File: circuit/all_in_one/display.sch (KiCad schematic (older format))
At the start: 8 parts, among them U10 IN-14, U11 IN-14, U12 IN-14, U13 IN-14, U14 IN-14, U15 IN-14, U16 IN-14, U17 IN-14

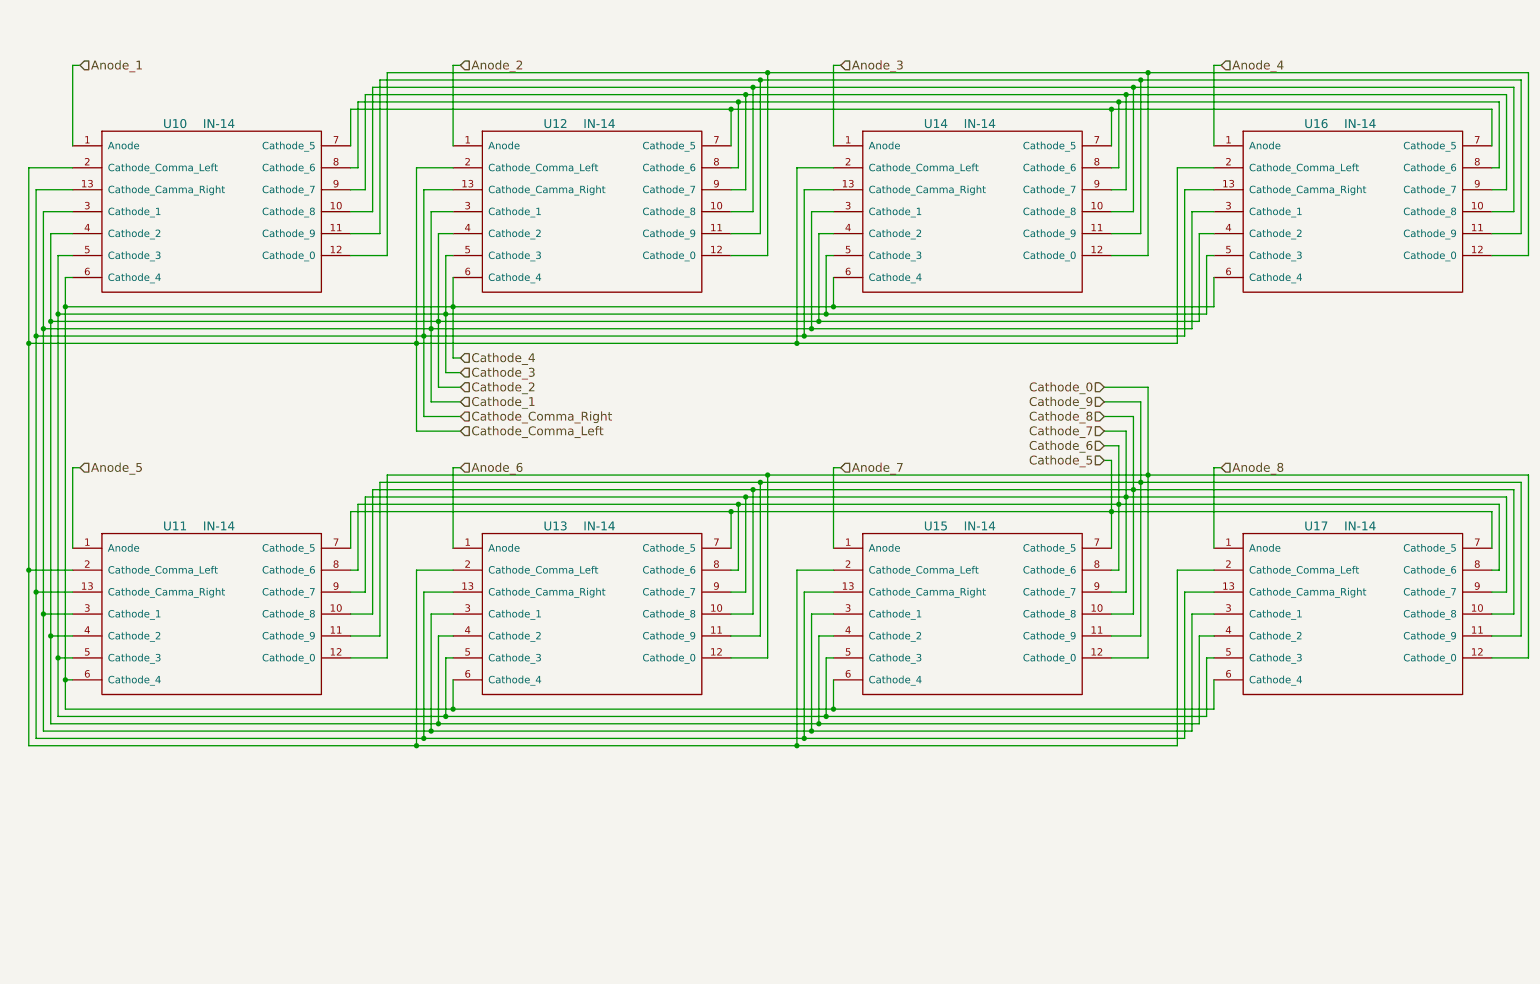
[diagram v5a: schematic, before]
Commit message: Finsihed placing all the components
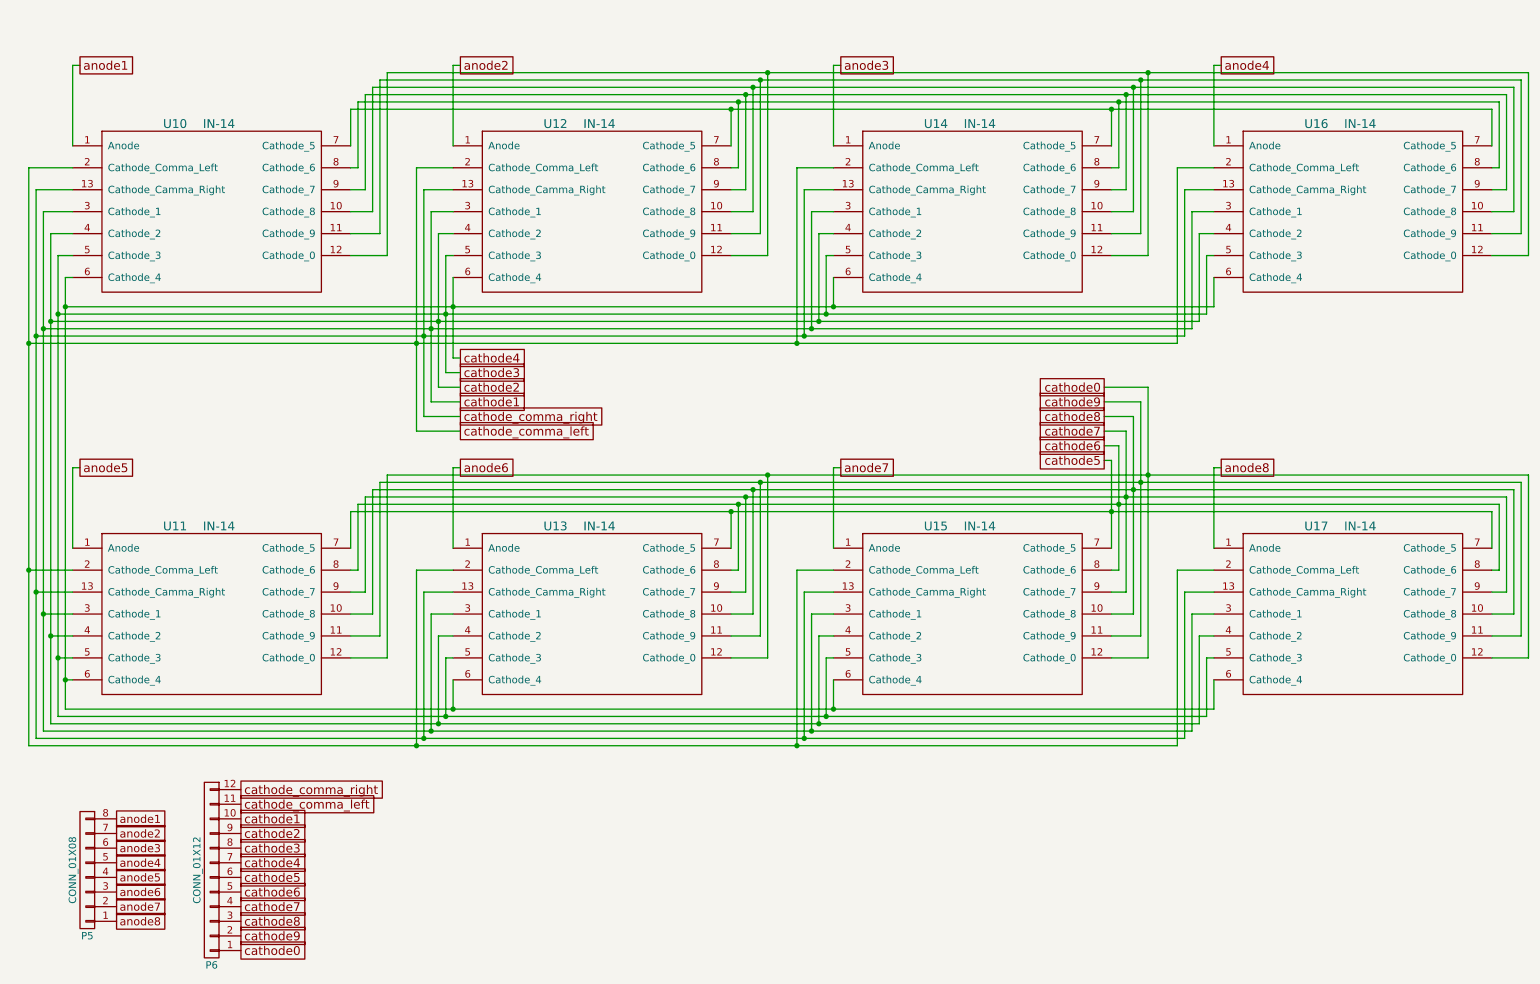
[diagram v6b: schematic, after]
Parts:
- added P5: CONN_01X08, Pin_Headers:Pin_Header_Straight_1x08, symbol CONN_01X08
- added P6: CONN_01X12, Pin_Headers:Pin_Header_Straight_1x12, symbol CONN_01X12
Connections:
- net Anode_1 renamed anode1
- net anode1: now also P5.8 (P8)
- net Anode_2 renamed anode2
- net anode2: now also P5.7 (P7)
- net Anode_3 renamed anode3
- net anode3: now also P5.6 (P6)
- net Anode_4 renamed anode4
- net anode4: now also P5.5 (P5)
- net Anode_5 renamed anode5
- net anode5: now also P5.4 (P4)
- net Anode_6 renamed anode6
- net anode6: now also P5.3 (P3)
- net Anode_7 renamed anode7
- net anode7: now also P5.2 (P2)
- net Anode_8 renamed anode8
- net anode8: now also P5.1 (P1)
- net Cathode_0 renamed cathode0
- net cathode0: now also P6.1 (P1)
- net Cathode_1 renamed cathode1
- net cathode1: now also P6.10 (P10)
- net Cathode_2 renamed cathode2
- net cathode2: now also P6.9 (P9)
- net Cathode_3 renamed cathode3
- net cathode3: now also P6.8 (P8)
- net Cathode_4 renamed cathode4
- net cathode4: now also P6.7 (P7)
- net Cathode_5 renamed cathode5
- net cathode5: now also P6.6 (P6)
- net Cathode_6 renamed cathode6
- net cathode6: now also P6.5 (P5)
- net Cathode_7 renamed cathode7
- net cathode7: now also P6.4 (P4)
- net Cathode_8 renamed cathode8
- net cathode8: now also P6.3 (P3)
- net Cathode_9 renamed cathode9
- net cathode9: now also P6.2 (P2)
- net Cathode_Comma_Left renamed cathode_comma_left
- net cathode_comma_left: now also P6.11 (P11)
- net Cathode_Comma_Right renamed cathode_comma_right
- net cathode_comma_right: now also P6.12 (P12)
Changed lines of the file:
@@
 $Descr A4 11693 8268
 encoding utf-8
-Sheet 6 6
+Sheet 6 5
 Title ""
 Date ""
@@
 Wire Wire Line
 	3150 5250 3150 4000
-Wire Wire Line
-	3150 4000 10950 4000
 Wire Wire Line
 	5750 4000 5750 5250
@@
 Wire Wire Line
 	3600 1750 3600 1200
-Text HLabel 3650 1200 2    60   Input ~ 0
-Anode_2
 Wire Wire Line
 	3600 1200 3650 1200
 Wire Wire Line
 	1000 1750 1000 1200
-Text HLabel 1050 1200 2    60   Input ~ 0
-Anode_1
 Wire Wire Line
 	1000 1200 1050 1200
 Wire Wire Line
 	6200 1750 6200 1200
-Text HLabel 6250 1200 2    60   Input ~ 0
-Anode_3
 Wire Wire Line
 	6200 1200 6250 1200
 Wire Wire Line
 	8800 1750 8800 1200
-Text HLabel 8850 1200 2    60   Input ~ 0
-Anode_4
 Wire Wire Line
 	8800 1200 8850 1200
 Wire Wire Line
 	1000 4500 1000 3950
-Text HLabel 1050 3950 2    60   Input ~ 0
-Anode_5
 Wire Wire Line
 	1000 3950 1050 3950
 Wire Wire Line
 	3600 4500 3600 3950
-Text HLabel 3650 3950 2    60   Input ~ 0
-Anode_6
 Wire Wire Line
 	3600 3950 3650 3950
 Wire Wire Line
 	6200 4500 6200 3950
-Text HLabel 6250 3950 2    60   Input ~ 0
-Anode_7
 Wire Wire Line
 	6200 3950 6250 3950
 Wire Wire Line
 	8800 4500 8800 3950
-Text HLabel 8850 3950 2    60   Input ~ 0
-Anode_8
 Wire Wire Line
 	8800 3950 8850 3950
-Text HLabel 3650 3200 2    60   Input ~ 0
-Cathode_4
-Text HLabel 3650 3300 2    60   Input ~ 0
-Cathode_3
 Wire Wire Line
 	3600 3200 3650 3200
 Wire Wire Line
 	3550 3300 3650 3300
-Text HLabel 3650 3400 2    60   Input ~ 0
-Cathode_2
-Text HLabel 3650 3500 2    60   Input ~ 0
-Cathode_1
-Text HLabel 3650 3600 2    60   Input ~ 0
-Cathode_Comma_Right
-Text HLabel 3650 3700 2    60   Input ~ 0
-Cathode_Comma_Left
 Wire Wire Line
 	3500 3400 3650 3400
@@
 Wire Wire Line
 	3350 3700 3650 3700
-Text HLabel 8050 3900 0    60   Input ~ 0
-Cathode_5
-Text HLabel 8050 3800 0    60   Input ~ 0
-Cathode_6
-Text HLabel 8050 3700 0    60   Input ~ 0
-Cathode_7
-Text HLabel 8050 3600 0    60   Input ~ 0
-Cathode_8
-Text HLabel 8050 3500 0    60   Input ~ 0
-Cathode_9
-Text HLabel 8050 3400 0    60   Input ~ 0
-Cathode_0
 Wire Wire Line
 	8100 3900 8050 3900
@@
 Wire Wire Line
 	700  3100 8550 3100
+Text GLabel 1050 1200 2    60   UnSpc ~ 0
+anode1
+Text GLabel 3650 1200 2    60   UnSpc ~ 0
+anode2
+Text GLabel 6250 1200 2    60   UnSpc ~ 0
+anode3
+Text GLabel 8850 1200 2    60   UnSpc ~ 0
+anode4
+Text GLabel 1050 3950 2    60   UnSpc ~ 0
+anode5
+Text GLabel 3650 3950 2    60   UnSpc ~ 0
+anode6
+Text GLabel 6250 3950 2    60   UnSpc ~ 0
+anode7
+Text GLabel 8850 3950 2    60   UnSpc ~ 0
+anode8
+Wire Wire Line
+	3150 4000 10950 4000
+$Comp
+L CONN_01X08 P5
+U 1 1 56A3C4CF
+P 1100 6700
+F 0 "P5" H 1100 7150 50  0000 C CNN
+F 1 "CONN_01X08" V 1200 6700 50  0000 C CNN
+F 2 "Pin_Headers:Pin_Header_Straight_1x08" H 1100 6700 50  0001 C CNN
+F 3 "" H 1100 6700 50  0000 C CNN
+	1    1100 6700
+	-1   0    0    1
+$EndComp
+Text GLabel 1300 6350 2    55   UnSpc ~ 0
+anode1
+Text GLabel 1300 6450 2    55   UnSpc ~ 0
+anode2
+Text GLabel 1300 6550 2    55   UnSpc ~ 0
+anode3
+Text GLabel 1300 6650 2    55   UnSpc ~ 0
+anode4
+Text GLabel 1300 6750 2    55   UnSpc ~ 0
+anode5
+Text GLabel 1300 6850 2    55   UnSpc ~ 0
+anode6
+Text GLabel 1300 6950 2    55   UnSpc ~ 0
+anode7
+Text GLabel 1300 7050 2    55   UnSpc ~ 0
+anode8
+Text GLabel 8050 3400 0    60   UnSpc ~ 0
+cathode0
+Text GLabel 8050 3500 0    60   UnSpc ~ 0
+cathode9
+Text GLabel 8050 3600 0    60   UnSpc ~ 0
+cathode8
+Text GLabel 8050 3700 0    60   UnSpc ~ 0
+cathode7
+Text GLabel 8050 3800 0    60   UnSpc ~ 0
+cathode6
+Text GLabel 8050 3900 0    60   UnSpc ~ 0
+cathode5
+Text GLabel 3650 3200 2    60   UnSpc ~ 0
+cathode4
+Text GLabel 3650 3300 2    60   UnSpc ~ 0
+cathode3
+Text GLabel 3650 3400 2    60   UnSpc ~ 0
+cathode2
+Text GLabel 3650 3500 2    60   UnSpc ~ 0
+cathode1
+Text GLabel 3650 3600 2    60   UnSpc ~ 0
+cathode_comma_right
+Text GLabel 3650 3700 2    60   UnSpc ~ 0
+cathode_comma_left
+$Comp
+L CONN_01X12 P6
+U 1 1 56A3E427
+P 1950 6700
+F 0 "P6" H 1950 7350 50  0000 C CNN
+F 1 "CONN_01X12" V 2050 6700 50  0000 C CNN
+F 2 "Pin_Headers:Pin_Header_Straight_1x12" H 1950 6700 50  0001 C CNN
+F 3 "" H 1950 6700 50  0000 C CNN
+	1    1950 6700
+	-1   0    0    1
+$EndComp
+Text GLabel 2150 7250 2    60   UnSpc ~ 0
+cathode0
+Text GLabel 2150 7150 2    60   UnSpc ~ 0
+cathode9
+Text GLabel 2150 7050 2    60   UnSpc ~ 0
+cathode8
+Text GLabel 2150 6950 2    60   UnSpc ~ 0
+cathode7
+Text GLabel 2150 6850 2    60   UnSpc ~ 0
+cathode6
+Text GLabel 2150 6750 2    60   UnSpc ~ 0
+cathode5
+Text GLabel 2150 6650 2    60   UnSpc ~ 0
+cathode4
+Text GLabel 2150 6550 2    60   UnSpc ~ 0
+cathode3
+Text GLabel 2150 6450 2    60   UnSpc ~ 0
+cathode2
+Text GLabel 2150 6350 2    60   UnSpc ~ 0
+cathode1
+Text GLabel 2150 6250 2    60   UnSpc ~ 0
+cathode_comma_left
+Text GLabel 2150 6150 2    60   UnSpc ~ 0
+cathode_comma_right
 $EndSCHEMATC
